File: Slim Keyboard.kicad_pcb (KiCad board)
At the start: 2 copper layers, 26 x 45.5 mm, 58 parts, among them J1 USB_C_Receptacle_USB2.0_16P, J2 SWD, J3 SWC, J5 S2B-PH-SM4-TB, U1 NRF52840-QIAA-R, U2 BQ24075RGT, U3 XC6220B331MR, Y1 ECS-.327-9-34B-TR, Y2 XRCGB32M000F1S2KR0

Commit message: Routing
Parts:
- J2, J3: moved to F.Cu
- moved J2 17.8 mm to (76.5, 71.8), turned to 90 degrees
- moved J3 13.6 mm to (79.0, 71.8), turned to 90 degrees
- moved J5 1.26 mm to (82.2, 45.4)
- moved C19 1.04 mm to (76.8, 62.5)
- moved C5 1.04 mm to (76.8, 61.0)
- moved C20 0.75 mm to (78.2, 58.0)
- moved C21 0.75 mm to (78.2, 56.5)
- moved L5 0.75 mm to (78.2, 59.5), turned to 180 degrees
- moved R3 0.75 mm to (84.8, 55.0)
- moved R10 0.51 mm to (83.0, 50.6)
- moved R2 0.39 mm to (82.8, 52.8)
- moved C22 0.30 mm to (83.5, 51.8)
- moved R11 0.30 mm to (83.5, 53.8)
- moved C26 0.25 mm to (78.5, 49.8)
- moved R6 0.25 mm to (76.5, 49.8)
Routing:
- net VDDH: track 7.59 -> 37.2 mm
- net D-: track 0.00 -> 28.1 mm, vias 0 -> 2
- net D+: track 0.00 -> 24.4 mm, vias 0 -> 4
- net RESET: track 0.00 -> 23.6 mm, vias 0 -> 1
- net Net-(J1-SHIELD): track 0.00 -> 20.0 mm
- net EXT_VCC: track 0.50 -> 16.7 mm
- net VDD_NRF: track 0.00 -> 15.3 mm
- net SYSOFF_SWITCH: track 0.00 -> 13.6 mm
- net VBUS: track 1.39 -> 13.2 mm, vias 0 -> 3
- net Net-(U1-DEC4): track 0.00 -> 10.0 mm
- net Net-(U1-P0.00/XL1): track 0.00 -> 8.14 mm
- net Net-(U1-XC1): track 0.00 -> 7.25 mm
- net GND: track 6.03 -> 12.0 mm, vias 7 -> 15
- net Net-(U1-XC2): track 0.00 -> 5.28 mm
- net Net-(AE1-A): track 0.00 -> 4.91 mm
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
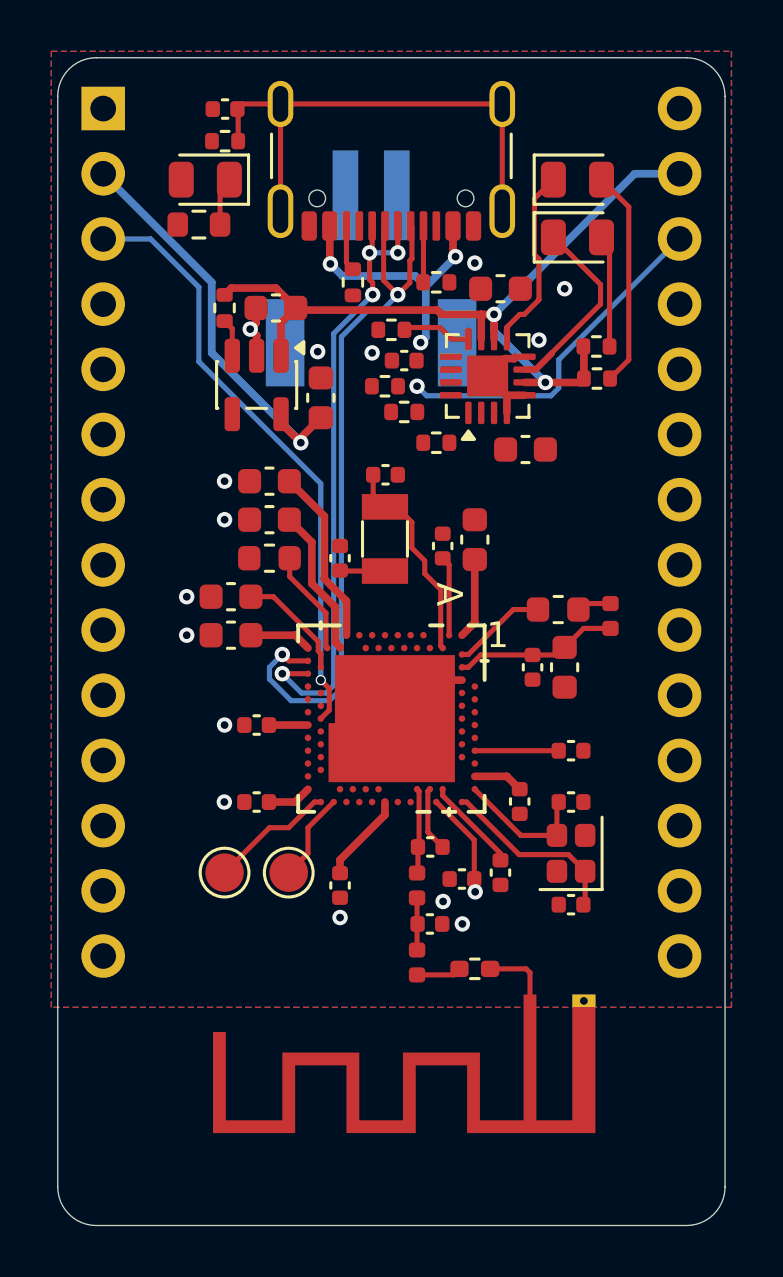
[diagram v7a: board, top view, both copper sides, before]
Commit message: Routing Done; DFM problems to solve
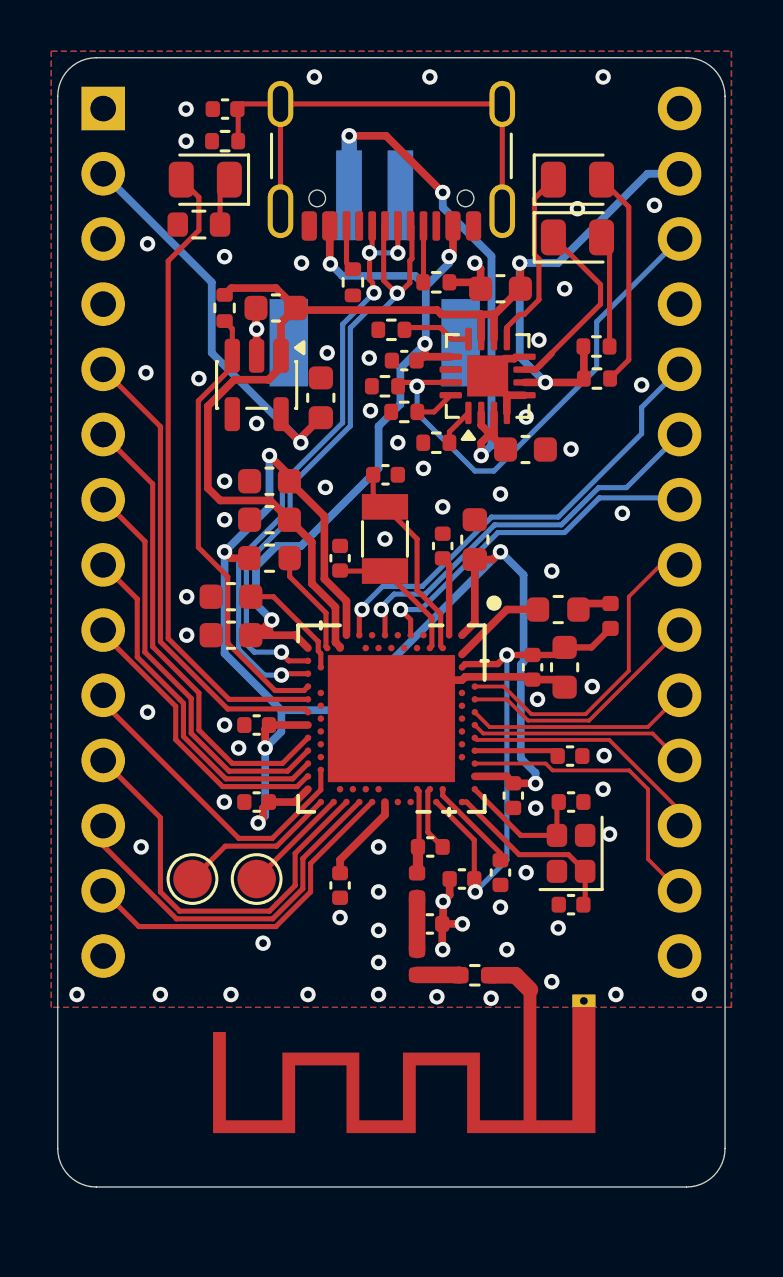
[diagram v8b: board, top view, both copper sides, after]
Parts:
- moved J2 1.27 mm to (75.2, 72.0)
- moved J3 1.27 mm to (77.8, 72.0)
- moved C6 0.34 mm to (87.8, 68.8)
- moved R1 0.25 mm to (86.2, 75.8)
- moved C10 0.21 mm to (90.0, 67.2)
- moved J5 0.14 mm to (82.3, 45.4)
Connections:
- J7 pad 14: PH9 -> unconnected-(J7-x-Pad14)
- J7 pad 15: PL10 -> unconnected-(J7-x-Pad15)
- J7 pad 16: PL11 -> PH9
- J7 pad 17: PL12 -> PL10
- J7 pad 18: PL13 -> PL11
- J7 pad 19: PL14 -> PL12
- J7 pad 20: PL15 -> PL13
- J7 pad 21: PL16 -> PL14
- J7 pad 22: PL17 -> PL15
- J7 pad 23: PL18 -> PL16
- J7 pad 24: PL19 -> PL17
- U1 pad A10: PL17 -> PL13
- U1 pad A12: PL15 -> PL12
- U1 pad A14: PL13 -> PL11
- U1 pad A16: PL11 -> PL10
- U1 pad A20: unconnected-(U1-P1.10-PadA20) -> PH9
- U1 pad A8: PL19 -> PL14
- U1 pad AC11: PH0 -> unconnected-(U1-P0.16-PadAC11)
- U1 pad AC13: RESET -> unconnected-(U1-P0.18/NRESET-PadAC13)
- U1 pad AC15: PH2 -> unconnected-(U1-P0.19-PadAC15)
- U1 pad AC17: PH4 -> unconnected-(U1-P0.21-PadAC17)
- U1 pad AC19: PH6 -> unconnected-(U1-P0.23-PadAC19)
- U1 pad AC21: PH8 -> PH5
- U1 pad AD12: PH1 -> PH0
- U1 pad AD16: PH3 -> PH1
- U1 pad AD18: PH5 -> PH2
- U1 pad AD20: PH7 -> PH3
- U1 pad AD22: PH9 -> PH4
- U1 pad B11: PL16 -> unconnected-(U1-P0.28/AIN4-PadB11)
- U1 pad B13: PL14 -> unconnected-(U1-P0.03/AIN1-PadB13)
- U1 pad B15: PL12 -> unconnected-(U1-P1.14-PadB15)
- U1 pad B17: PL10 -> unconnected-(U1-P1.12-PadB17)
- U1 pad B9: PL18 -> unconnected-(U1-P0.30/AIN6-PadB9)
- U1 pad J1: unconnected-(U1-P0.04/AIN2-PadJ1) -> PL15
- U1 pad N1: unconnected-(U1-P0.08-PadN1) -> PL16
- U1 pad R24: unconnected-(U1-P1.06-PadR24) -> PH8
- U1 pad U1: unconnected-(U1-P0.12-PadU1) -> PL17
- U1 pad U24: unconnected-(U1-P1.04-PadU24) -> PH7
- U1 pad W24: unconnected-(U1-P1.02-PadW24) -> PH6
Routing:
- net VDD_NRF: track 15.3 -> 58.4 mm, vias 0 -> 6
- net BLED: track 0.00 -> 25.1 mm
- net RESET: track 23.6 -> 0.00 mm, vias 1 -> 0
- net VBAT: track 0.00 -> 21.9 mm, vias 0 -> 3
- net PH0: track 0.00 -> 18.4 mm
- net PH1: track 0.00 -> 18.3 mm
- net PL17: track 0.00 -> 18.0 mm, vias 0 -> 1
- net VBUS: track 13.2 -> 30.7 mm, vias 3 -> 4
- net POWER_PIN: track 1.55 -> 17.7 mm
- net PH6: track 0.00 -> 16.1 mm
- net PH2: track 0.00 -> 16.0 mm
- net PL16: track 0.00 -> 15.6 mm, vias 0 -> 1
- net PH7: track 0.00 -> 14.5 mm
- net PL15: track 0.00 -> 13.9 mm, vias 0 -> 1
- net PH3: track 0.00 -> 13.8 mm
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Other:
- board size 26 x 45.5 mm -> 26 x 44 mm
